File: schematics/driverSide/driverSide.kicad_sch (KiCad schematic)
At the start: 46 parts, among them J1 Conn_01x20, J10 Conn_01x20, J11 Conn_01x20, J12 Conn_01x20, J13 Conn_01x20, J14 Conn_01x20, J15 Conn_01x20, J16 Conn_01x20, J17 Conn_01x20, J18 Conn_01x20, J19 PINHD_1x8_Male, J2 OLEDdisp, J20 PINHD_1x8_Male, J21 Conn_01x02, J22 Screw_Terminal_01x02, J3 Rotencoder, J4 Conn_01x20, J5 Conn_01x20, J6 Conn_01x20, J7 Conn_01x20, J8 Conn_01x20, J9 Conn_01x20, SW1 Push_Button, U1 PC817, U2 4046, U3 UCC37322, U4 UCC37322

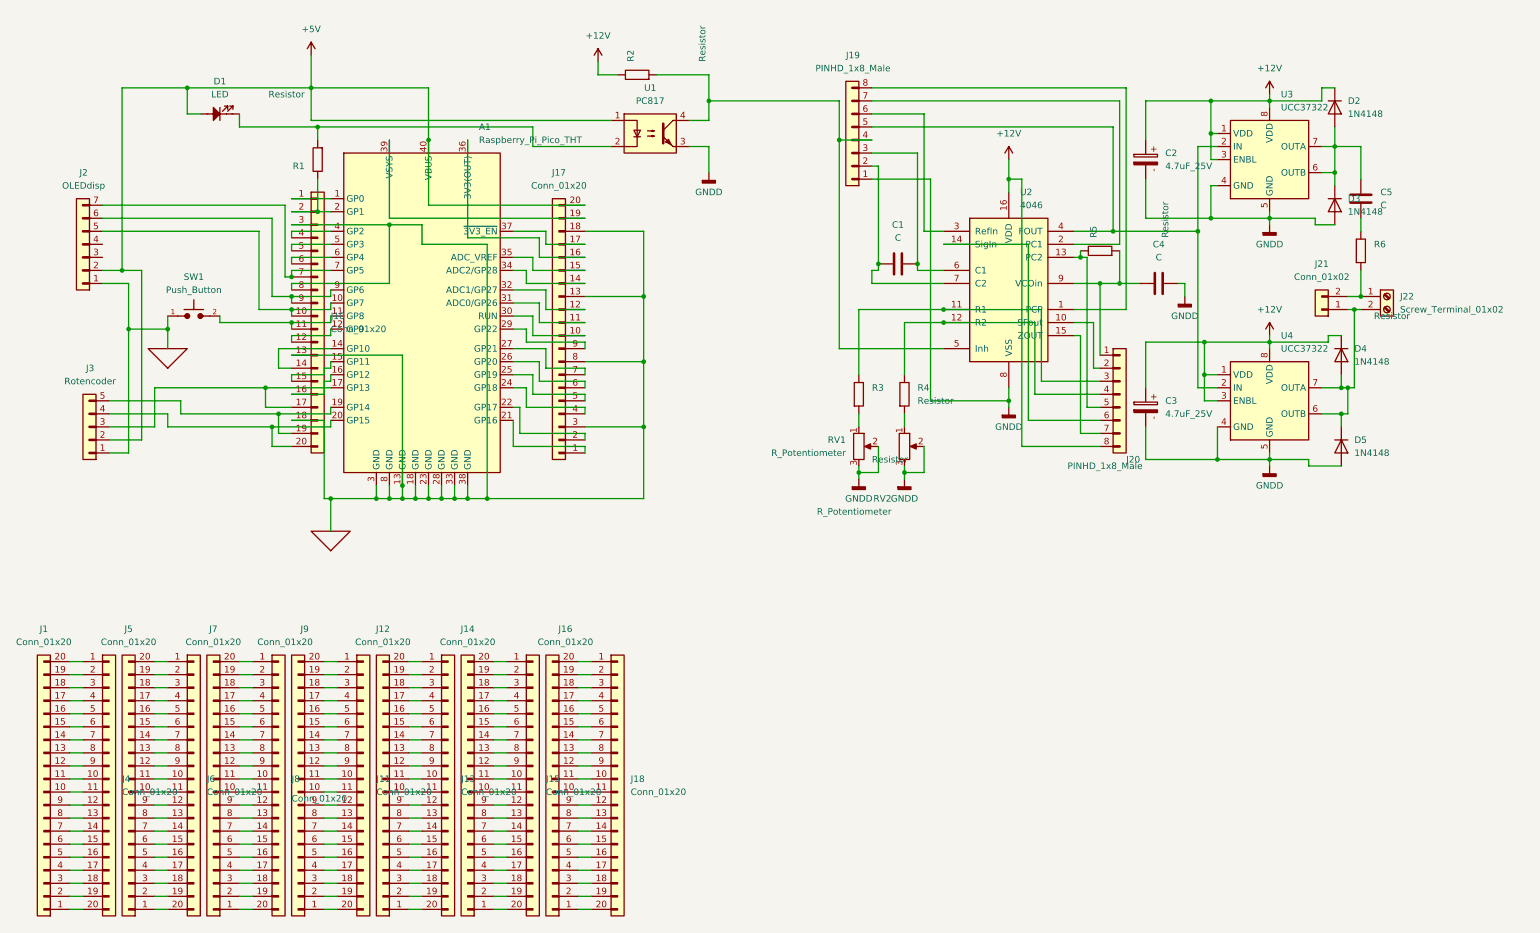
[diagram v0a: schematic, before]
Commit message: first version driver board completed
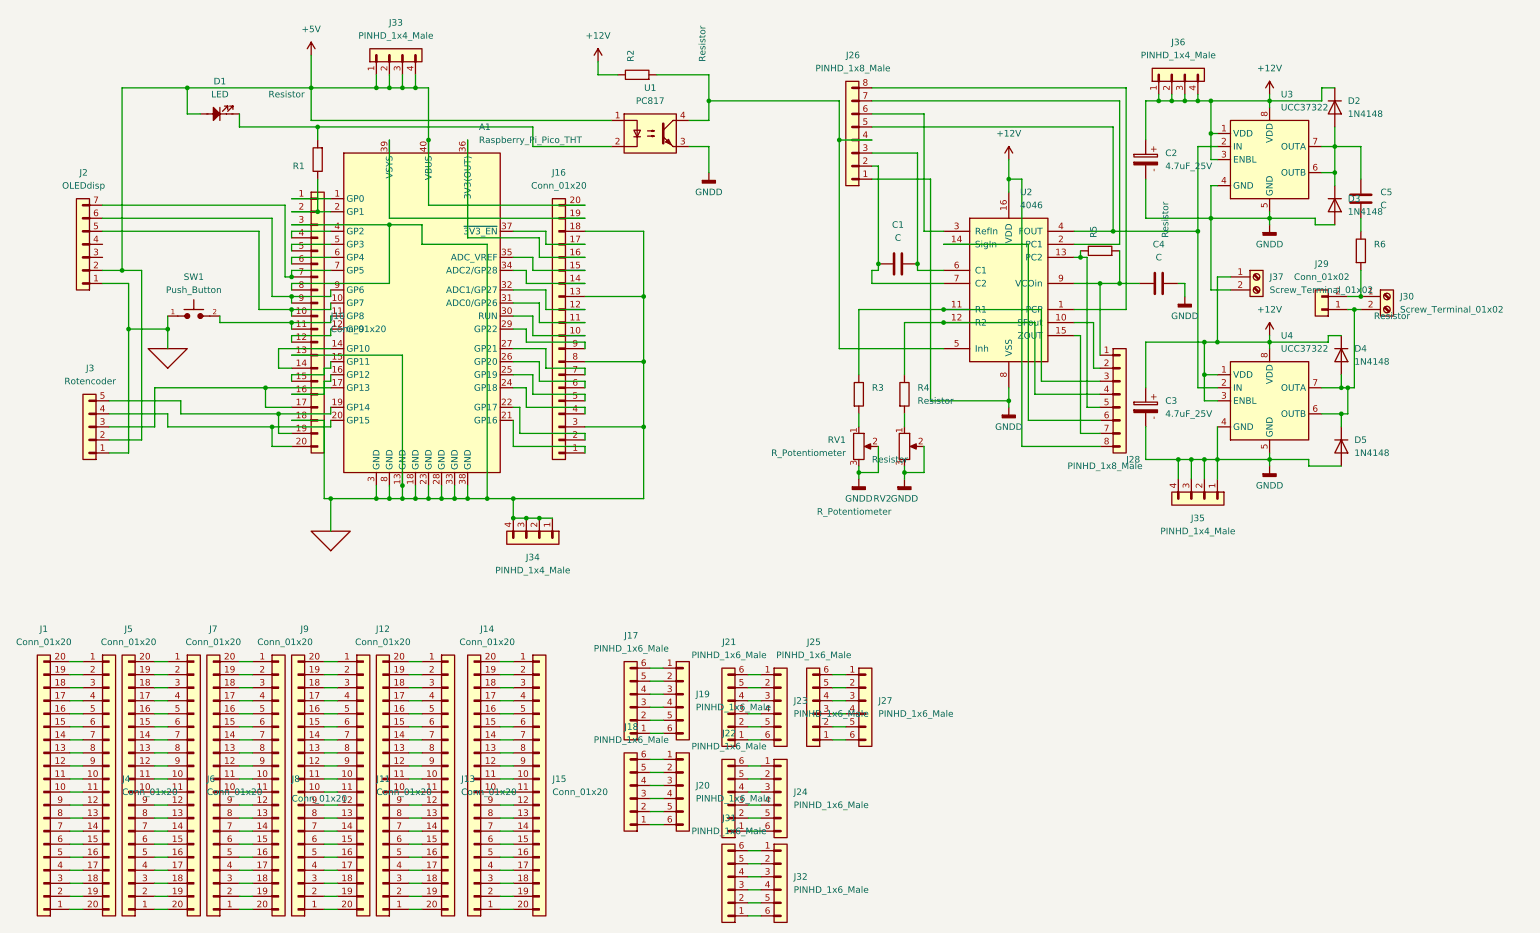
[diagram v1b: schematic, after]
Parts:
- removed J14, J15: Conn_01x20, Connector_PinHeader_2.54mm:PinHeader_1x20_P2.54mm_Vertical, symbol Connector_Generic:Conn_01x20
- added J17, J18, J19, J20, J21, J22, J23, J24, J25, J27, J31, J32: PINHD_1x6_Male, Connector_PinHeader_2.54mm:PinHeader_1x06_P2.54mm_Vertical, symbol PCM_SL_Pin_Headers:PINHD_1x6_Male
- added J33, J34, J35, J36: PINHD_1x4_Male, Connector_PinHeader_2.54mm:PinHeader_1x04_P2.54mm_Vertical, symbol PCM_SL_Pin_Headers:PINHD_1x4_Male
- added J37: Screw_Terminal_01x02, TerminalBlock:TerminalBlock_bornier-2_P5.08mm, symbol Connector:Screw_Terminal_01x02
- renumbered J16 to J14, J18 to J15, J17 to J16, J19 to J26, J20 to J28, J21 to J29, J22 to J30
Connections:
- net +12V: now also J36.1, J36.2, J36.3, J36.4, J37.1 (Pin_1)
- net +5V: now also J33.1, J33.2, J33.3, J33.4
- net GND: now also J34.1, J34.2, J34.3, J34.4
- net GNDD: now also J35.1, J35.2, J35.3, J35.4, J37.2 (Pin_2)
- new net: J31.1, J32.6
- new net: J31.2, J32.5
- new net: J31.3, J32.4
- new net: J31.4, J32.3
- new net: J31.5, J32.2
- new net: J31.6, J32.1
- new net: J25.1, J27.6
- new net: J25.2, J27.5
- new net: J25.3, J27.4
- new net: J25.4, J27.3
- new net: J25.5, J27.2
- new net: J25.6, J27.1
- new net: J18.6, J20.1
- new net: J18.5, J20.2
- new net: J18.4, J20.3
- new net: J18.3, J20.4
- new net: J18.2, J20.5
- new net: J18.1, J20.6
- new net: J21.1, J23.6
- new net: J21.2, J23.5
- new net: J21.3, J23.4
- new net: J21.4, J23.3
- new net: J21.5, J23.2
- new net: J21.6, J23.1
- new net: J17.1, J19.6
- new net: J17.2, J19.5
- new net: J17.3, J19.4
- new net: J17.4, J19.3
- new net: J17.5, J19.2
- new net: J17.6, J19.1
- new net: J22.6, J24.1
- new net: J22.5, J24.2
- new net: J22.4, J24.3
- new net: J22.3, J24.4
- new net: J22.2, J24.5
- new net: J22.1, J24.6
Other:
- moved on the sheet: J14, J15
